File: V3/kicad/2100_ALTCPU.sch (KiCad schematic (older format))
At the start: 23 parts, among them U1 74HCT273, U2100 Z8-L180-S180-180-PQFP-80, U2101 GAL16V8, U2102 14.7456 MHz

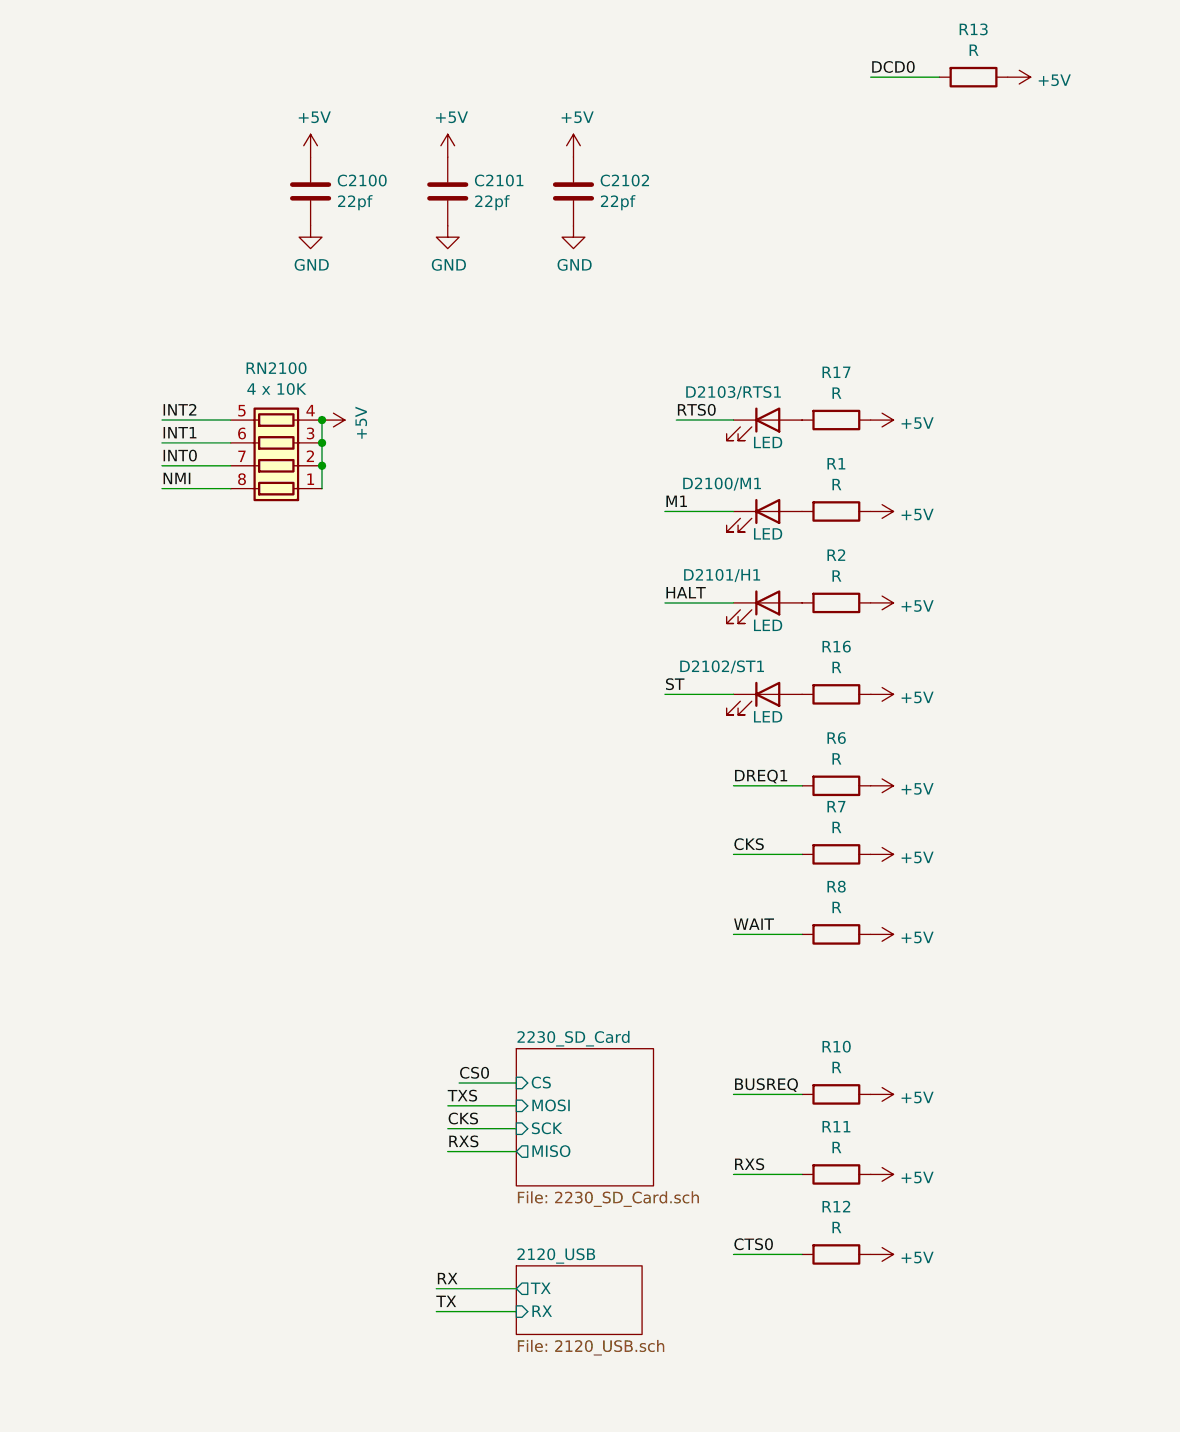
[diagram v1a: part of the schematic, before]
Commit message: Added one more r array
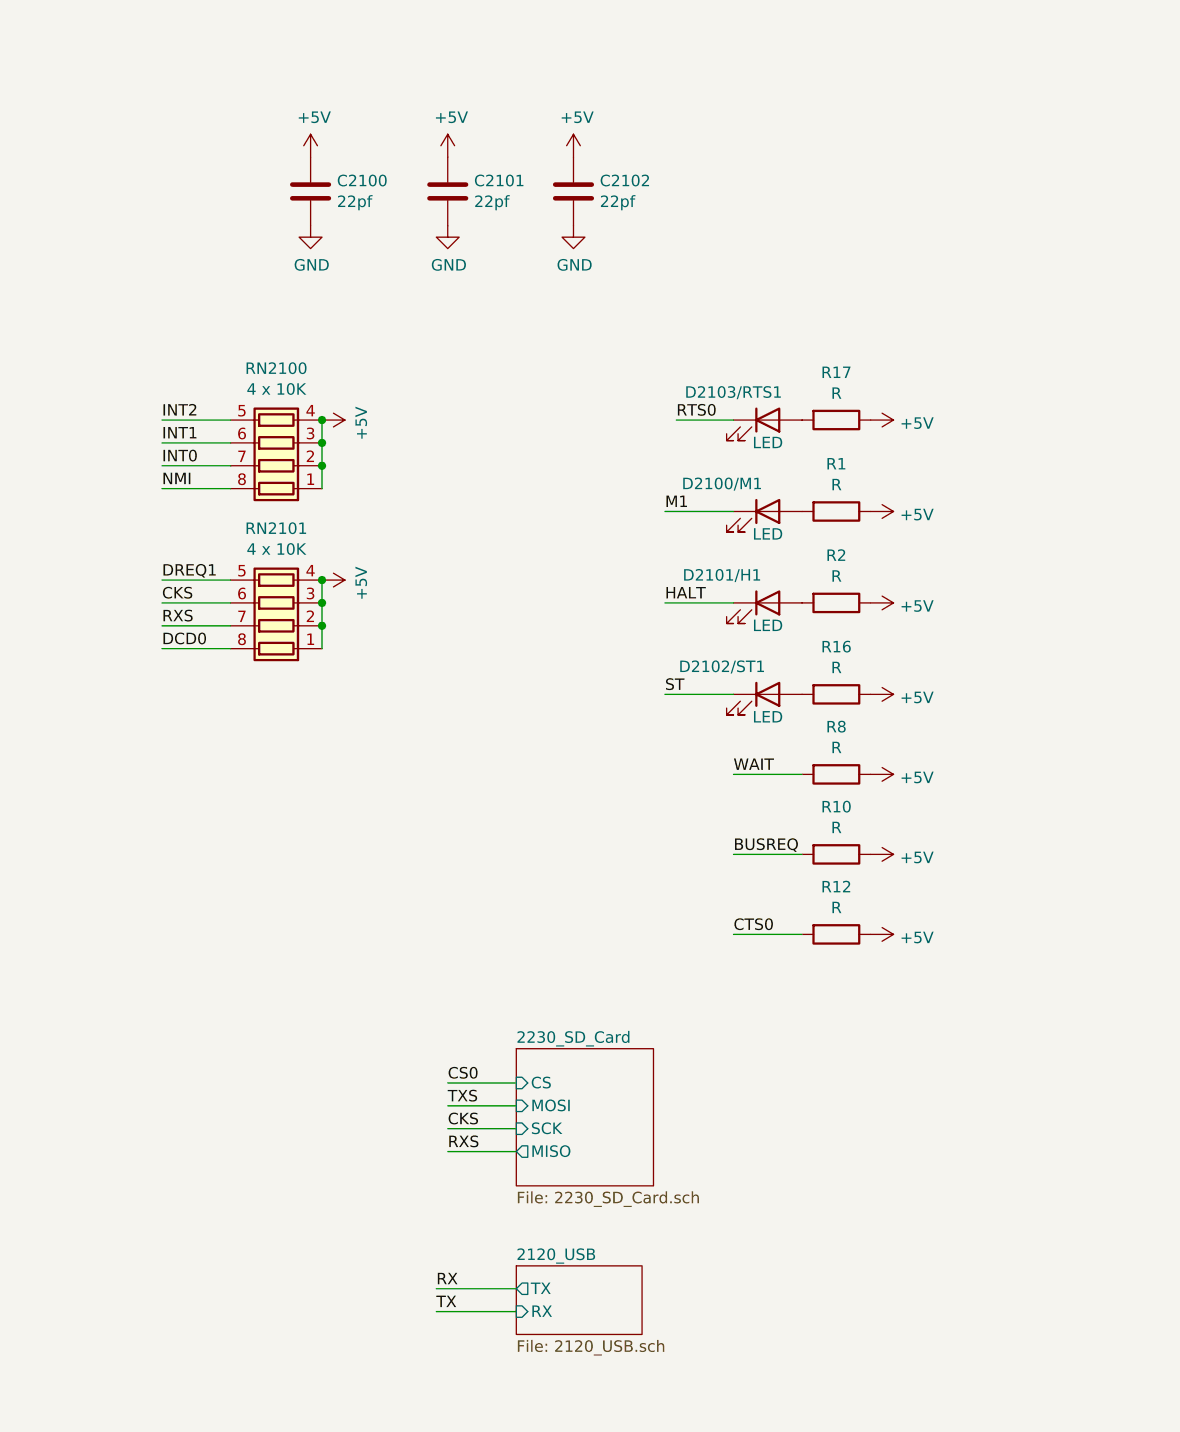
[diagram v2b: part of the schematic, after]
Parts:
- removed R11, R13, R6, R7: R, Resistor_SMD:R_1206_3216Metric, symbol Device:R
- added RN2101: 4 x 10K, Resistor_SMD:R_Array_Convex_4x1206, symbol Device:R_Pack04
- U1: footprint (none) -> Package_SO:SOIC-20W_7.5x12.8mm_P1.27mm
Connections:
- net +5V: now also RN2101.1 (R1.1), RN2101.2 (R2.1), RN2101.3 (R3.1), RN2101.4 (R4.1)
- net CKS: now also RN2101.6 (R3.2)
- net DCD0: now also RN2101.8 (R1.2)
- net DREQ1: now also RN2101.5 (R4.2)
- net RXS: now also RN2101.7 (R2.2)
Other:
- moved on the sheet: R10, R12, R8
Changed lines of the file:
@@
 WAIT
 Wire Wire Line
-	9750 5200 9450 5200
-Text Label 9450 5200 0    50   ~ 0
+	9750 4150 9450 4150
+Text Label 9450 4150 0    50   ~ 0
 BUSREQ
 Wire Wire Line
-	9750 4500 9450 4500
-Text Label 9450 4500 0    50   ~ 0
+	9750 3800 9450 3800
+Text Label 9450 3800 0    50   ~ 0
 WAIT
 Text HLabel 4450 3000 2    50   Output ~ 0
@@
 CTS0
 Wire Wire Line
-	9750 5900 9450 5900
-Text Label 9450 5900 0    50   ~ 0
+	9750 4500 9450 4500
+Text Label 9450 4500 0    50   ~ 0
 CTS0
 Wire Wire Line
-	9750 3850 9450 3850
-Text Label 9450 3850 0    50   ~ 0
+	7250 2950 6950 2950
+Text Label 6950 2950 0    50   ~ 0
 DREQ1
 Wire Wire Line
@@
 Text Label 1700 4550 0    50   ~ 0
 DCD0
-Wire Wire Line
-	10350 750  10050 750
-Text Label 10050 750  0    50   ~ 0
-DCD0
 NoConn ~ 3700 5350
 Text Label 4450 2300 2    50   ~ 0
@@
 NoConn ~ 4150 4300
 Wire Wire Line
-	9750 5550 9450 5550
-Text Label 9450 5550 0    50   ~ 0
-RXS
-Wire Wire Line
-	9750 4150 9450 4150
-Text Label 9450 4150 0    50   ~ 0
+	7250 3050 6950 3050
+Text Label 6950 3050 0    50   ~ 0
 CKS
 Wire Wire Line
@@
 $EndComp
 $Comp
-L Device:R R6
-U 1 1 62EE459D
-P 9900 3850
-F 0 "R6" V 9693 3850 50  0000 C CNN
-F 1 "R" V 9784 3850 50  0000 C CNN
-F 2 "Resistor_SMD:R_1206_3216Metric" V 9830 3850 50  0001 C CNN
-F 3 "~" H 9900 3850 50  0001 C CNN
-	1    9900 3850
-	0    1    1    0
-$EndComp
-$Comp
-L power:+5V #PWR0122
-U 1 1 62EE45A3
-P 10050 3850
-F 0 "#PWR0122" H 10050 3700 50  0001 C CNN
-F 1 "+5V" V 10065 3978 50  0000 L CNN
-F 2 "" H 10050 3850 50  0001 C CNN
-F 3 "" H 10050 3850 50  0001 C CNN
-	1    10050 3850
-	0    1    1    0
-$EndComp
-$Comp
-L Device:R R7
-U 1 1 62EEEA1B
+L Device:R R8
+U 1 1 62EF9277
+P 9900 3800
+F 0 "R8" V 9693 3800 50  0000 C CNN
+F 1 "R" V 9784 3800 50  0000 C CNN
+F 2 "Resistor_SMD:R_1206_3216Metric" V 9830 3800 50  0001 C CNN
+F 3 "~" H 9900 3800 50  0001 C CNN
+	1    9900 3800
+	0    1    1    0
+$EndComp
+$Comp
+L power:+5V #PWR0136
+U 1 1 62EF927D
+P 10050 3800
+F 0 "#PWR0136" H 10050 3650 50  0001 C CNN
+F 1 "+5V" V 10065 3928 50  0000 L CNN
+F 2 "" H 10050 3800 50  0001 C CNN
+F 3 "" H 10050 3800 50  0001 C CNN
+	1    10050 3800
+	0    1    1    0
+$EndComp
+$Comp
+L Device:R R10
+U 1 1 62F00BDB
 P 9900 4150
-F 0 "R7" V 9693 4150 50  0000 C CNN
+F 0 "R10" V 9693 4150 50  0000 C CNN
 F 1 "R" V 9784 4150 50  0000 C CNN
 F 2 "Resistor_SMD:R_1206_3216Metric" V 9830 4150 50  0001 C CNN
@@
 $EndComp
 $Comp
-L power:+5V #PWR0135
-U 1 1 62EEEA21
+L power:+5V #PWR0138
+U 1 1 62F00BE1
 P 10050 4150
-F 0 "#PWR0135" H 10050 4000 50  0001 C CNN
+F 0 "#PWR0138" H 10050 4000 50  0001 C CNN
 F 1 "+5V" V 10065 4278 50  0000 L CNN
 F 2 "" H 10050 4150 50  0001 C CNN
@@
 $EndComp
 $Comp
-L Device:R R8
-U 1 1 62EF9277
+L Device:R R12
+U 1 1 62F0767B
 P 9900 4500
-F 0 "R8" V 9693 4500 50  0000 C CNN
+F 0 "R12" V 9693 4500 50  0000 C CNN
 F 1 "R" V 9784 4500 50  0000 C CNN
 F 2 "Resistor_SMD:R_1206_3216Metric" V 9830 4500 50  0001 C CNN
@@
 $EndComp
 $Comp
-L power:+5V #PWR0136
-U 1 1 62EF927D
+L power:+5V #PWR0140
+U 1 1 62F07681
 P 10050 4500
-F 0 "#PWR0136" H 10050 4350 50  0001 C CNN
+F 0 "#PWR0140" H 10050 4350 50  0001 C CNN
 F 1 "+5V" V 10065 4628 50  0000 L CNN
 F 2 "" H 10050 4500 50  0001 C CNN
 F 3 "" H 10050 4500 50  0001 C CNN
 	1    10050 4500
-	0    1    1    0
-$EndComp
-$Comp
-L Device:R R10
-U 1 1 62F00BDB
-P 9900 5200
-F 0 "R10" V 9693 5200 50  0000 C CNN
-F 1 "R" V 9784 5200 50  0000 C CNN
-F 2 "Resistor_SMD:R_1206_3216Metric" V 9830 5200 50  0001 C CNN
-F 3 "~" H 9900 5200 50  0001 C CNN
-	1    9900 5200
-	0    1    1    0
-$EndComp
-$Comp
-L power:+5V #PWR0138
-U 1 1 62F00BE1
-P 10050 5200
-F 0 "#PWR0138" H 10050 5050 50  0001 C CNN
-F 1 "+5V" V 10065 5328 50  0000 L CNN
-F 2 "" H 10050 5200 50  0001 C CNN
-F 3 "" H 10050 5200 50  0001 C CNN
-	1    10050 5200
-	0    1    1    0
-$EndComp
-$Comp
-L Device:R R11
-U 1 1 62F03FB9
-P 9900 5550
-F 0 "R11" V 9693 5550 50  0000 C CNN
-F 1 "R" V 9784 5550 50  0000 C CNN
-F 2 "Resistor_SMD:R_1206_3216Metric" V 9830 5550 50  0001 C CNN
-F 3 "~" H 9900 5550 50  0001 C CNN
-	1    9900 5550
-	0    1    1    0
-$EndComp
-$Comp
-L power:+5V #PWR0139
-U 1 1 62F03FBF
-P 10050 5550
-F 0 "#PWR0139" H 10050 5400 50  0001 C CNN
-F 1 "+5V" V 10065 5678 50  0000 L CNN
-F 2 "" H 10050 5550 50  0001 C CNN
-F 3 "" H 10050 5550 50  0001 C CNN
-	1    10050 5550
-	0    1    1    0
-$EndComp
-$Comp
-L Device:R R12
-U 1 1 62F0767B
-P 9900 5900
-F 0 "R12" V 9693 5900 50  0000 C CNN
-F 1 "R" V 9784 5900 50  0000 C CNN
-F 2 "Resistor_SMD:R_1206_3216Metric" V 9830 5900 50  0001 C CNN
-F 3 "~" H 9900 5900 50  0001 C CNN
-	1    9900 5900
-	0    1    1    0
-$EndComp
-$Comp
-L power:+5V #PWR0140
-U 1 1 62F07681
-P 10050 5900
-F 0 "#PWR0140" H 10050 5750 50  0001 C CNN
-F 1 "+5V" V 10065 6028 50  0000 L CNN
-F 2 "" H 10050 5900 50  0001 C CNN
-F 3 "" H 10050 5900 50  0001 C CNN
-	1    10050 5900
-	0    1    1    0
-$EndComp
-$Comp
-L Device:R R13
-U 1 1 62F0AE91
-P 10500 750
-F 0 "R13" V 10293 750 50  0000 C CNN
-F 1 "R" V 10384 750 50  0000 C CNN
-F 2 "Resistor_SMD:R_1206_3216Metric" V 10430 750 50  0001 C CNN
-F 3 "~" H 10500 750 50  0001 C CNN
-	1    10500 750
-	0    1    1    0
-$EndComp
-$Comp
-L power:+5V #PWR0141
-U 1 1 62F0AE97
-P 10650 750
-F 0 "#PWR0141" H 10650 600 50  0001 C CNN
-F 1 "+5V" V 10665 878 50  0000 L CNN
-F 2 "" H 10650 750 50  0001 C CNN
-F 3 "" H 10650 750 50  0001 C CNN
-	1    10650 750
 	0    1    1    0
 $EndComp
@@
 Wire Wire Line
 	9150 2650 9450 2650
-Text Label 8250 5150 0    50   ~ 0
+Text Label 8200 5150 0    50   ~ 0
 CS0
-Wire Wire Line
-	8250 5150 8500 5150
 Wire Wire Line
 	4150 4700 4450 4700
@@
 F 0 "U1" H 4750 7600 50  0000 C CNN
 F 1 "74HCT273" H 4750 7500 50  0000 C CNN
-F 2 "" H 4450 6750 50  0001 C CNN
+F 2 "Package_SO:SOIC-20W_7.5x12.8mm_P1.27mm" H 4450 6750 50  0001 C CNN
 F 3 "https://assets.nexperia.com/documents/data-sheet/74HC_HCT273.pdf" H 4450 6750 50  0001 C CNN
 	1    4450 6750
@@
 Text Label 6950 2550 0    50   ~ 0
 NMI
+$Comp
+L Device:R_Pack04 RN?
+U 1 1 639E8FD4
+P 7450 3050
+AR Path="/6191B6A2/61EBDADB/636B5B34/639E8FD4" Ref="RN?"  Part="1"
+AR Path="/6191B6A2/61EBDADB/639E8FD4" Ref="RN2101"  Part="1"
+F 0 "RN2101" V 7775 3050 50  0000 C CNN
+F 1 "4 x 10K" V 7684 3050 50  0000 C CNN
+F 2 "Resistor_SMD:R_Array_Convex_4x1206" V 7725 3050 50  0001 C CNN
+F 3 "~" H 7450 3050 50  0001 C CNN
+	1    7450 3050
+	0    -1   -1   0
+$EndComp
+Wire Wire Line
+	7250 3150 6950 3150
+Text Label 6950 3150 0    50   ~ 0
+RXS
+Wire Wire Line
+	7250 3250 6950 3250
+Text Label 6950 3250 0    50   ~ 0
+DCD0
+$Comp
+L power:+5V #PWR?
+U 1 1 63A14D5D
+P 7650 2950
+AR Path="/6195D2C9/63A14D5D" Ref="#PWR?"  Part="1"
+AR Path="/6191B6A2/61F28B7D/63A14D5D" Ref="#PWR?"  Part="1"
+AR Path="/6191B6A2/61EBDADB/63A14D5D" Ref="#PWR0122"  Part="1"
+F 0 "#PWR0122" H 7650 2800 50  0001 C CNN
+F 1 "+5V" H 7665 3123 50  0000 C CNN
+F 2 "" H 7650 2950 50  0001 C CNN
+F 3 "" H 7650 2950 50  0001 C CNN
+	1    7650 2950
+	0    1    1    0
+$EndComp
+Wire Wire Line
+	7650 2950 7650 3050
+Connection ~ 7650 2950
+Connection ~ 7650 3050
+Wire Wire Line
+	7650 3050 7650 3150
+Connection ~ 7650 3150
+Wire Wire Line
+	7650 3150 7650 3250
+Wire Wire Line
+	8200 5150 8500 5150
 Wire Bus Line
 	1700 3150 1700 3850
